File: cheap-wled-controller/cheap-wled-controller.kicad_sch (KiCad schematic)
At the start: 47 parts, among them J10 Conn_01x05_Pin, J2 USB_C_Receptacle, J4 Conn_02x05_Odd_Even, J6 Conn_01x05_Pin, J7 Conn_01x02_Pin, J8 Conn_01x07_Pin, Q3 NMOS, SW1 SW_Push, U1 USBLC6-2SC6, U3 CH224K, U4 MX5014S, U5 ESP32-S3-WROOM-1-N4R2, U7 TPS54202DDC, U9 AMS1117-3.3

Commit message: pcb fixes
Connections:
- no-connect marks 21 -> 39
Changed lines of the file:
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@@
+	)
+	(no_connect
+		(at 34.29 199.39)
+	)
+	(no_connect
+		(at 243.84 66.04)
 	)
 	(no_connect
@@
 	)
 	(no_connect
+		(at 57.15 195.58)
+	)
+	(no_connect
+		(at 34.29 194.31)
+	)
+	(no_connect
+		(at 34.29 204.47)
+	)
+	(no_connect
+		(at 57.15 162.56)
+	)
+	(no_connect
 		(at 41.91 71.12)
 	)
 	(no_connect
+		(at 34.29 196.85)
+	)
+	(no_connect
 		(at 41.91 101.6)
 	)
 	(no_connect
+		(at 34.29 153.67)
+	)
+	(no_connect
 		(at 66.04 58.42)
 	)
@@
 	)
 	(no_connect
+		(at 34.29 171.45)
+	)
+	(no_connect
+		(at 34.29 176.53)
+	)
+	(no_connect
+		(at 57.15 203.2)
+	)
+	(no_connect
+		(at 34.29 201.93)
+	)
+	(no_connect
 		(at 41.91 68.58)
 	)
@@
 	)
 	(no_connect
+		(at 34.29 189.23)
+	)
+	(no_connect
 		(at 41.91 83.82)
 	)
@@
 	)
 	(no_connect
+		(at 57.15 193.04)
+	)
+	(no_connect
+		(at 34.29 173.99)
+	)
+	(no_connect
+		(at 57.15 200.66)
+	)
+	(no_connect
 		(at 129.54 190.5)
 	)
+	(no_connect
+		(at 34.29 191.77)
+	)
+	(no_connect
+		(at 57.15 154.94)
+	)
 	(wire
 		(pts
@@
 	(wire
 		(pts
+			(xy 62.23 182.88) (xy 57.15 182.88)
+		)
+		(stroke
+			(width 0)
+			(type default)
+		)
+	)
+	(wire
+		(pts
 			(xy 226.06 85.09) (xy 232.41 85.09)
 		)
@@
 	(wire
 		(pts
+			(xy 62.23 172.72) (xy 57.15 172.72)
+		)
+		(stroke
+			(width 0)
+			(type default)
+		)
+	)
+	(wire
+		(pts
 			(xy 115.57 138.43) (xy 115.57 139.7)
 		)
@@
 	(wire
 		(pts
+			(xy 62.23 185.42) (xy 57.15 185.42)
+		)
+		(stroke
+			(width 0)
+			(type default)
+		)
+	)
+	(wire
+		(pts
 			(xy 120.65 151.13) (xy 115.57 151.13)
 		)
@@
 	(wire
 		(pts
+			(xy 62.23 170.18) (xy 57.15 170.18)
+		)
+		(stroke
+			(width 0)
+			(type default)
+		)
+	)
+	(wire
+		(pts
 			(xy 96.52 101.6) (xy 96.52 96.52)
 		)
@@
 	(wire
 		(pts
+			(xy 62.23 177.8) (xy 57.15 177.8)
+		)
+		(stroke
+			(width 0)
+			(type default)
+		)
+	)
+	(wire
+		(pts
 			(xy 179.07 63.5) (xy 181.61 63.5)
 		)
@@
 	(wire
 		(pts
+			(xy 62.23 180.34) (xy 57.15 180.34)
+		)
+		(stroke
+			(width 0)
+			(type default)
+		)
+	)
+	(wire
+		(pts
 			(xy 226.06 85.09) (xy 226.06 86.36)
 		)
@@
 	(wire
 		(pts
+			(xy 62.23 187.96) (xy 57.15 187.96)
+		)
+		(stroke
+			(width 0)
+			(type default)
+		)
+	)
+	(wire
+		(pts
 			(xy 219.71 66.04) (xy 220.98 66.04)
 		)
@@
 		(pts
 			(xy 215.9 73.66) (xy 219.71 73.66)
+		)
+		(stroke
+			(width 0)
+			(type default)
+		)
+	)
+	(wire
+		(pts
+			(xy 62.23 175.26) (xy 57.15 175.26)
 		)
 		(stroke
@@
 	)
 	(label "GPIO37"
-		(at 57.15 182.88 0)
+		(at 62.23 182.88 0)
 		(effects
 			(font
@@
 	)
 	(label "GPIO41"
-		(at 57.15 172.72 0)
+		(at 62.23 172.72 0)
 		(effects
 			(font
@@
 	)
 	(label "GPIO35"
-		(at 57.15 187.96 0)
+		(at 62.23 187.96 0)
 		(effects
 			(font
@@
 	)
 	(label "GPIO42"
-		(at 57.15 170.18 0)
+		(at 62.23 170.18 0)
 		(effects
 			(font
@@
 	)
 	(label "GPIO39"
-		(at 57.15 177.8 0)
+		(at 62.23 177.8 0)
 		(effects
 			(font
@@
 	)
 	(label "GPIO40"
-		(at 57.15 175.26 0)
+		(at 62.23 175.26 0)
 		(effects
 			(font
@@
 	)
 	(label "GPIO38"
-		(at 57.15 180.34 0)
+		(at 62.23 180.34 0)
 		(effects
 			(font
@@
 	)
 	(label "GPIO36"
-		(at 57.15 185.42 0)
-		(effects
-			(font
+		(at 62.23 185.42 0)
+		(effects
+			(font

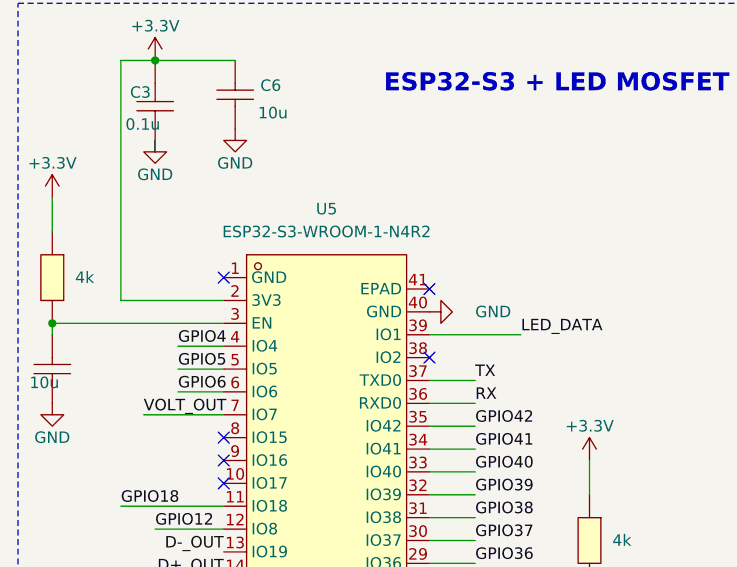
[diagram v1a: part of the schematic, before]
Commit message: added some GND for the esp32
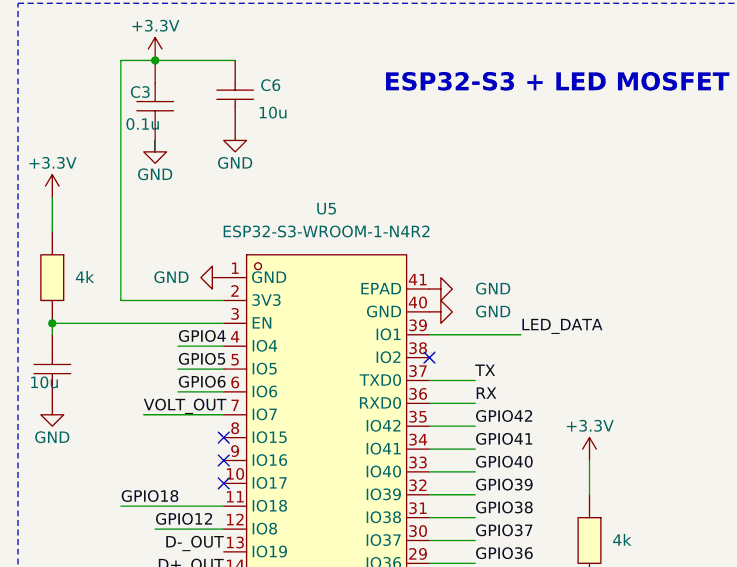
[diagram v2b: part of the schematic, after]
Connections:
- net GND: now also U5.1 (GND), U5.41 (EPAD)
- no-connect marks 39 -> 37
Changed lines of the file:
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@@
 	)
 	(no_connect
-		(at 34.29 153.67)
-	)
-	(no_connect
 		(at 66.04 58.42)
 	)
@@
 		(at 34.29 191.77)
 	)
-	(no_connect
-		(at 57.15 154.94)
-	)
 	(wire
 		(pts
@@
 	)
 	(symbol
+		(lib_id "power:GND")
+		(at 57.15 154.94 90)
+		(unit 1)
+		(exclude_from_sim no)
+		(in_bom yes)
+		(on_board yes)
+		(dnp no)
+		(fields_autoplaced yes)
+		(property "Reference" "#PWR02"
+			(at 63.5 154.94 0)
+			(effects
+				(font
+					(size 1.27 1.27)
+				)
+				(hide yes)
+			)
+		)
+		(property "Value" "GND"
+			(at 62.23 154.9399 90)
+			(effects
+				(font
+					(size 1.27 1.27)
+				)
+				(justify right)
+			)
+		)
+		(property "Footprint" ""
+			(at 57.15 154.94 0)
+			(effects
+				(font
+					(size 1.27 1.27)
+				)
+				(hide yes)
+			)
+		)
+		(property "Datasheet" ""
+			(at 57.15 154.94 0)
+			(effects
+				(font
+					(size 1.27 1.27)
+				)
+				(hide yes)
+			)
+		)
+		(property "Description" ""
+			(at 57.15 154.94 0)
+			(effects
+				(font
+					(size 1.27 1.27)
+				)
+				(hide yes)
+			)
+		)
+		(pin "1"
+		)
+		(instances
+			(project "cheap-wled-controller"
+				(path "/6a5d3644-22ac-4961-ba70-9807615c046f"
+					(reference "#PWR02")
+					(unit 1)
+				)
+			)
+		)
+	)
+	(symbol
 		(lib_id "power:+5V")
 		(at 205.74 153.67 0)
@@
 					(unit 1)
 				)
+			)
+		)
+	)
+	(symbol
+		(lib_id "power:GND")
+		(at 34.29 153.67 270)
+		(unit 1)
+		(exclude_from_sim no)
+		(in_bom yes)
+		(on_board yes)
+		(dnp no)
+		(fields_autoplaced yes)
+		(property "Reference" "#PWR03"
+			(at 27.94 153.67 0)
+			(effects
+				(font
+					(size 1.27 1.27)
+				)
+				(hide yes)
+			)
+		)
+		(property "Value" "GND"
+			(at 30.48 153.6699 90)
+			(effects
+				(font
+					(size 1.27 1.27)
+				)
+				(justify right)
+			)
+		)
+		(property "Footprint" ""
+			(at 34.29 153.67 0)
+			(effects
+				(font
+					(size 1.27 1.27)
+				)
+				(hide yes)
+			)
+		)
+		(property "Datasheet" ""
+			(at 34.29 153.67 0)
+			(effects
+				(font
+					(size 1.27 1.27)
+				)
+				(hide yes)
+			)
+		)
+		(property "Description" ""
+			(at 34.29 153.67 0)
+			(effects
+				(font
+					(size 1.27 1.27)
+				)
+				(hide yes)
+			)
+		)
+		(pin "1"
+		)
+		(instances
+			(project "cheap-wled-controller"
+				(path "/6a5d3644-22ac-4961-ba70-9807615c046f"
+					(reference "#PWR03")
+					(unit 1)
+				)

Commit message: new design mini 5x5
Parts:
- removed D4: LED_Small, cheap-wled-controller:LED0805-R-RD, symbol Device:LED_Small
- removed F2: DIR, cheap-wled-controller:FUSE-TH_XF-508P-A-B, symbol Device:Fuse_Small
- removed R12: 10k, cheap-wled-controller:R0805, symbol easyeda:0805W8F1002T5E
- added C4, C8: 10u, cheap-wled-controller:C0805, symbol easyeda:CL21A106KOQNNNE
- added C9: 1u, cheap-wled-controller:C0805, symbol easyeda:0805B105K500NT_C215803
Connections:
- net V_LED is gone; now on net VBUS_C: C1.2, Q3.2 (D), R15.2, U4.1 (V+)
- net +5V: now also C4.2, C8.2, C9.2
- net GND: now also C4.1, C8.1, C9.1
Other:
- note removed: "POWER STATUS LED"
- moved on the sheet: C29, C30, D2, L2, R13, R20, R22, U7, U9

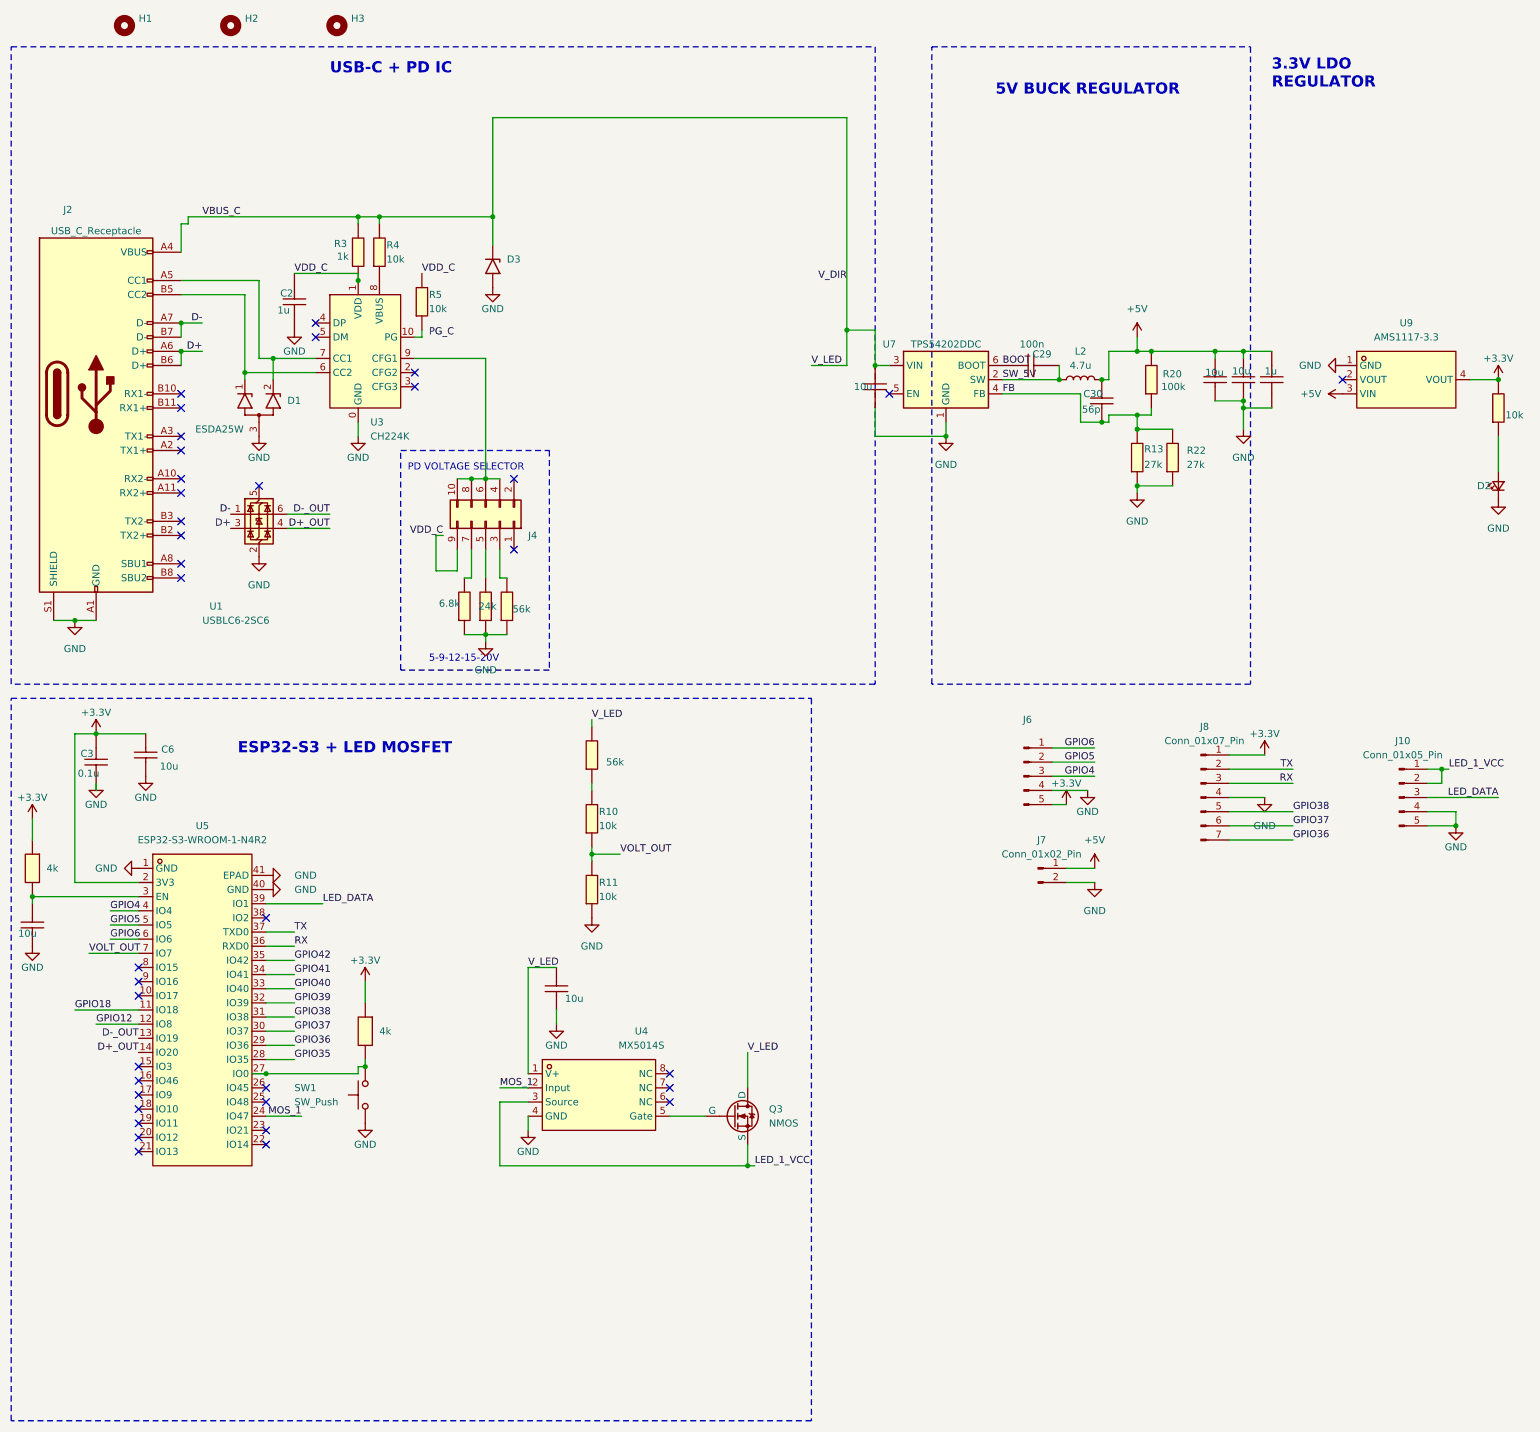
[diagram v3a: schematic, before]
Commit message: added capacitors for ams1117 and TSOP38238
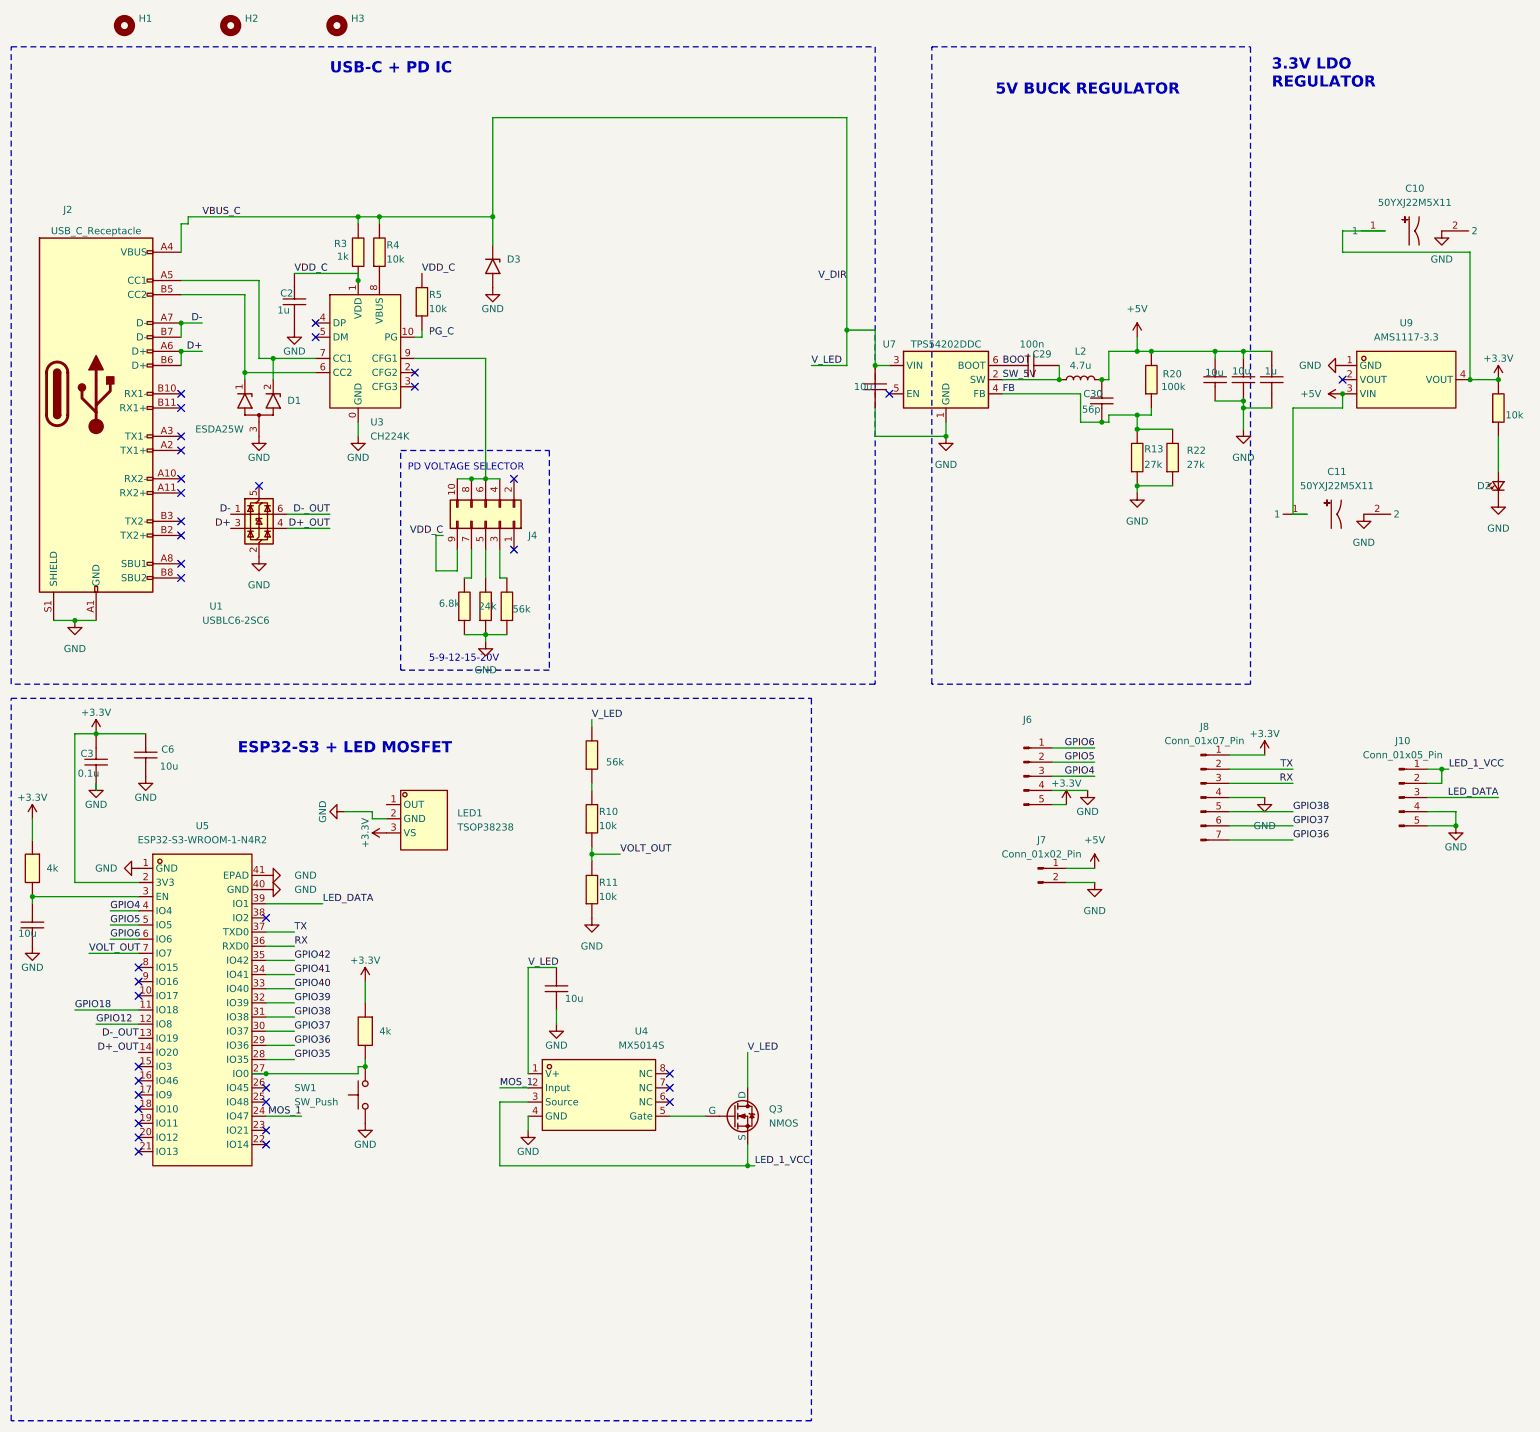
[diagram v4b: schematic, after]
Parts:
- added C10, C11: 50YXJ22M5X11, cheap-wled-controller:CAP-TH_BD5.0-P2.00-D0.5-FD-1, symbol easyeda:50YXJ22M5X11
- added LED1: TSOP38238, cheap-wled-controller:SENSOR-TG_TSOP38236, symbol easyeda:TSOP38238
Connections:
- net +3.3V: now also C10.1, LED1.3 (VS)
- net +5V: now also C11.1
- net GND: now also C10.2, C11.2, LED1.2 (GND)
